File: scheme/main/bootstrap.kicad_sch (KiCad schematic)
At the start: 7 parts, among them U1 B2415LS-1WR3

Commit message: replace some 220n capacitors with 100n
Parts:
- C13: value 220nF -> 100nF
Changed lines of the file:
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@@
 			)
 		)
-		(property "Value" "220nF"
+		(property "Value" "100nF"
 			(at 146.05 81.2799 0)
 			(effects

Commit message: sheets titles
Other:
- title: (none) -> Питание драйверов верхних ключей
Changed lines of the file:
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@@
 	(generator_version "8.0")
 	(paper "A4")
+	(title_block
+		(title "Питание драйверов верхних ключей")
+	)
 	(junction
 		(at 130.81 73.66)

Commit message: fixed check errors
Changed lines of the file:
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@@
+	(wire
+		(pts
+			(xy 142.24 71.12) (xy 142.24 73.66)
+		)
+		(stroke
+			(width 0)
+			(type default)
+		)
+	)
 	(wire
 		(pts
@@
 	)
 	(symbol
+		(lib_id "power:PWR_FLAG")
+		(at 142.24 71.12 0)
+		(unit 1)
+		(exclude_from_sim no)
+		(in_bom yes)
+		(on_board yes)
+		(dnp no)
+		(fields_autoplaced yes)
+		(property "Reference" "#FLG04"
+			(at 142.24 69.215 0)
+			(effects
+				(font
+					(size 1.27 1.27)
+				)
+				(hide yes)
+			)
+		)
+		(property "Value" "PWR_FLAG"
+			(at 142.24 66.04 0)
+			(effects
+				(font
+					(size 1.27 1.27)
+				)
+			)
+		)
+		(property "Footprint" ""
+			(at 142.24 71.12 0)
+			(effects
+				(font
+					(size 1.27 1.27)
+				)
+				(hide yes)
+			)
+		)
+		(property "Datasheet" "~"
+			(at 142.24 71.12 0)
+			(effects
+				(font
+					(size 1.27 1.27)
+				)
+				(hide yes)
+			)
+		)
+		(property "Description" "Special symbol for telling ERC where power comes from"
+			(at 142.24 71.12 0)
+			(effects
+				(font
+					(size 1.27 1.27)
+				)
+				(hide yes)
+			)
+		)
+		(pin "1"
+		)
+		(instances
+			(project ""
+				(path "/c11d1dbc-4db9-4712-8d1d-5f6f7086cded/5d407613-ca47-4478-86ea-137e1786be86/32b3c817-68f7-45e1-9258-7a9582664898"
+					(reference "#FLG02")
+					(unit 1)
+				)
+				(path "/c11d1dbc-4db9-4712-8d1d-5f6f7086cded/5d407613-ca47-4478-86ea-137e1786be86/c5b7b692-dec4-4ffa-a62b-cf474dae3f6f"
+					(reference "#FLG04")
+					(unit 1)
+				)
+				(path "/c11d1dbc-4db9-4712-8d1d-5f6f7086cded/5d407613-ca47-4478-86ea-137e1786be86/e7c7cf02-134e-4d37-ae3c-dbc1ef5b400e"
+					(reference "#FLG03")
+					(unit 1)
+				)
+			)
+		)
+	)
+	(symbol
 		(lib_id "Device:C")
 		(at 105.41 80.01 0)
@@
 		(dnp no)
 		(fields_autoplaced yes)
-		(property "Reference" "#PWR39"
+		(property "Reference" "#PWR039"
 			(at 66.04 92.71 0)
 			(effects
@@
 			(project ""
 				(path "/c11d1dbc-4db9-4712-8d1d-5f6f7086cded/5d407613-ca47-4478-86ea-137e1786be86/32b3c817-68f7-45e1-9258-7a9582664898"
-					(reference "#PWR39")
-					(unit 1)
-				)
-				(path "/c11d1dbc-4db9-4712-8d1d-5f6f7086cded/5d407613-ca47-4478-86ea-137e1786be86/c5b7b692-dec4-4ffa-a62b-cf474dae3f6f"
-					(reference "#PWR41")
-					(unit 1)
-				)
-				(path "/c11d1dbc-4db9-4712-8d1d-5f6f7086cded/5d407613-ca47-4478-86ea-137e1786be86/e7c7cf02-134e-4d37-ae3c-dbc1ef5b400e"
-					(reference "#PWR40")
+					(reference "#PWR039")
+					(unit 1)
+				)
+				(path "/c11d1dbc-4db9-4712-8d1d-5f6f7086cded/5d407613-ca47-4478-86ea-137e1786be86/c5b7b692-dec4-4ffa-a62b-cf474dae3f6f"
+					(reference "#PWR041")
+					(unit 1)
+				)
+				(path "/c11d1dbc-4db9-4712-8d1d-5f6f7086cded/5d407613-ca47-4478-86ea-137e1786be86/e7c7cf02-134e-4d37-ae3c-dbc1ef5b400e"
+					(reference "#PWR040")
 					(unit 1)
 				)
@@
 		(dnp no)
 		(fields_autoplaced yes)
-		(property "Reference" "#PWR36"
+		(property "Reference" "#PWR036"
 			(at 66.04 77.47 0)
 			(effects
@@
 			(project ""
 				(path "/c11d1dbc-4db9-4712-8d1d-5f6f7086cded/5d407613-ca47-4478-86ea-137e1786be86/32b3c817-68f7-45e1-9258-7a9582664898"
-					(reference "#PWR36")
-					(unit 1)
-				)
-				(path "/c11d1dbc-4db9-4712-8d1d-5f6f7086cded/5d407613-ca47-4478-86ea-137e1786be86/c5b7b692-dec4-4ffa-a62b-cf474dae3f6f"
-					(reference "#PWR38")
-					(unit 1)
-				)
-				(path "/c11d1dbc-4db9-4712-8d1d-5f6f7086cded/5d407613-ca47-4478-86ea-137e1786be86/e7c7cf02-134e-4d37-ae3c-dbc1ef5b400e"
-					(reference "#PWR37")
-					(unit 1)
-				)
+					(reference "#PWR036")
+					(unit 1)
+				)
+				(path "/c11d1dbc-4db9-4712-8d1d-5f6f7086cded/5d407613-ca47-4478-86ea-137e1786be86/c5b7b692-dec4-4ffa-a62b-cf474dae3f6f"
+					(reference "#PWR038")
+					(unit 1)
+				)
+				(path "/c11d1dbc-4db9-4712-8d1d-5f6f7086cded/5d407613-ca47-4478-86ea-137e1786be86/e7c7cf02-134e-4d37-ae3c-dbc1ef5b400e"
+					(reference "#PWR037")
+					(unit 1)
+				)

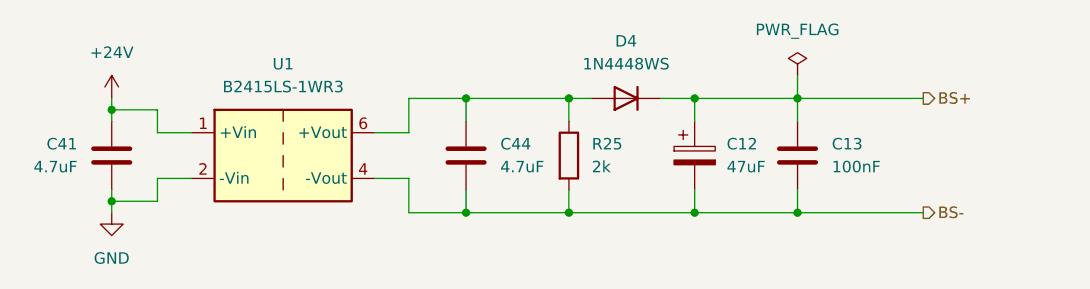
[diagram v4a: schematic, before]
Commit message: added capacitors to ipm power supply pin && added zener 20V to ipm bootstrap and power pins
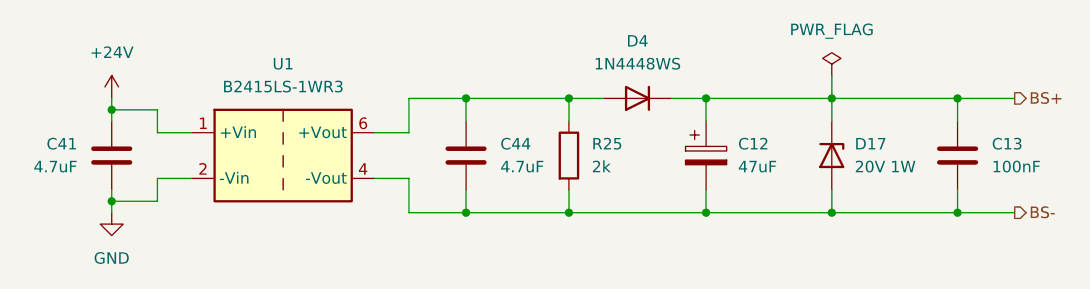
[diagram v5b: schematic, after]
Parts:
- added D17: 20V 1W, symbol Device:D_Zener
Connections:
- net BS+: now also D17.1 (K)
- net BS-: now also D17.2 (A)
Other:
- moved on the sheet: C12, C13, D4

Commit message: footprints set/changed
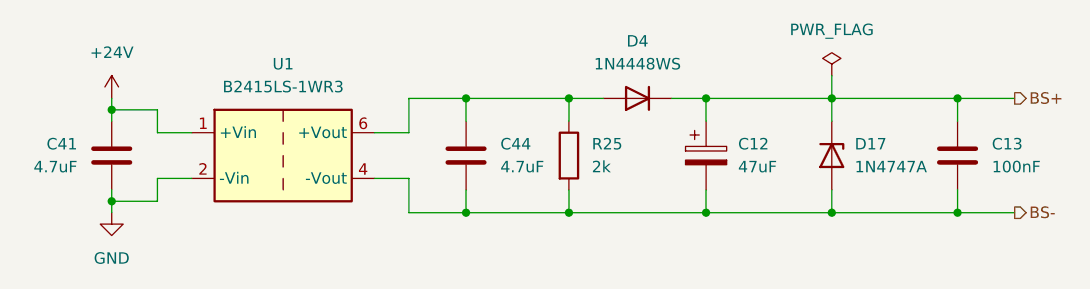
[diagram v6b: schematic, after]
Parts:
- D17: value 20V 1W -> 1N4747A; footprint (none) -> Diode_THT:D_DO-41_SOD81_P10.16mm_Horizontal
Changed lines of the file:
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@@
 			)
 		)
-		(property "Value" "20V 1W"
+		(property "Value" "1N4747A"
 			(at 148.59 81.2799 90)
 			(effects
@@
 			)
 		)
-		(property "Footprint" ""
+		(property "Footprint" "Diode_THT:D_DO-41_SOD81_P10.16mm_Horizontal"
 			(at 146.05 80.01 0)
 			(effects
@@
 			)
 		)
-		(property "Description" "Zener diode"
+		(property "Description" "20V 1W"
 			(at 146.05 80.01 0)
 			(effects
